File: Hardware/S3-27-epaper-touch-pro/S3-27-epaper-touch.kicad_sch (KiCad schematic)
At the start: 111 parts, among them J1 AFC24-S24FIC-00, J10 Conn_01x06_Pin, J2 Conn_01x06, J3 Conn_01x06, J4 TochConn, J5 Groove sensor, J6 Conn_01x05_Pin, J7 Conn_01x04_Pin, J8 Conn_01x06, Q1 Si1308, Q2 Si2301, SW1 SW_Push, SW2 SW_Push, SW3 SW_Push, SW4 SW_Push, SW5 SW_Push, SW6 SW_Push, SW7 SW_Push, SW8 SW_Push, SW9 SW_Push, U1 ESP32-S3-WROOM-1-N8, U2 RT9013, U3 KoreanHropartsElecTYPE-C-31-M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, U5 BME680, U6 TPL5110, U7 RFM95W-868S2, U8 LSM6DSL

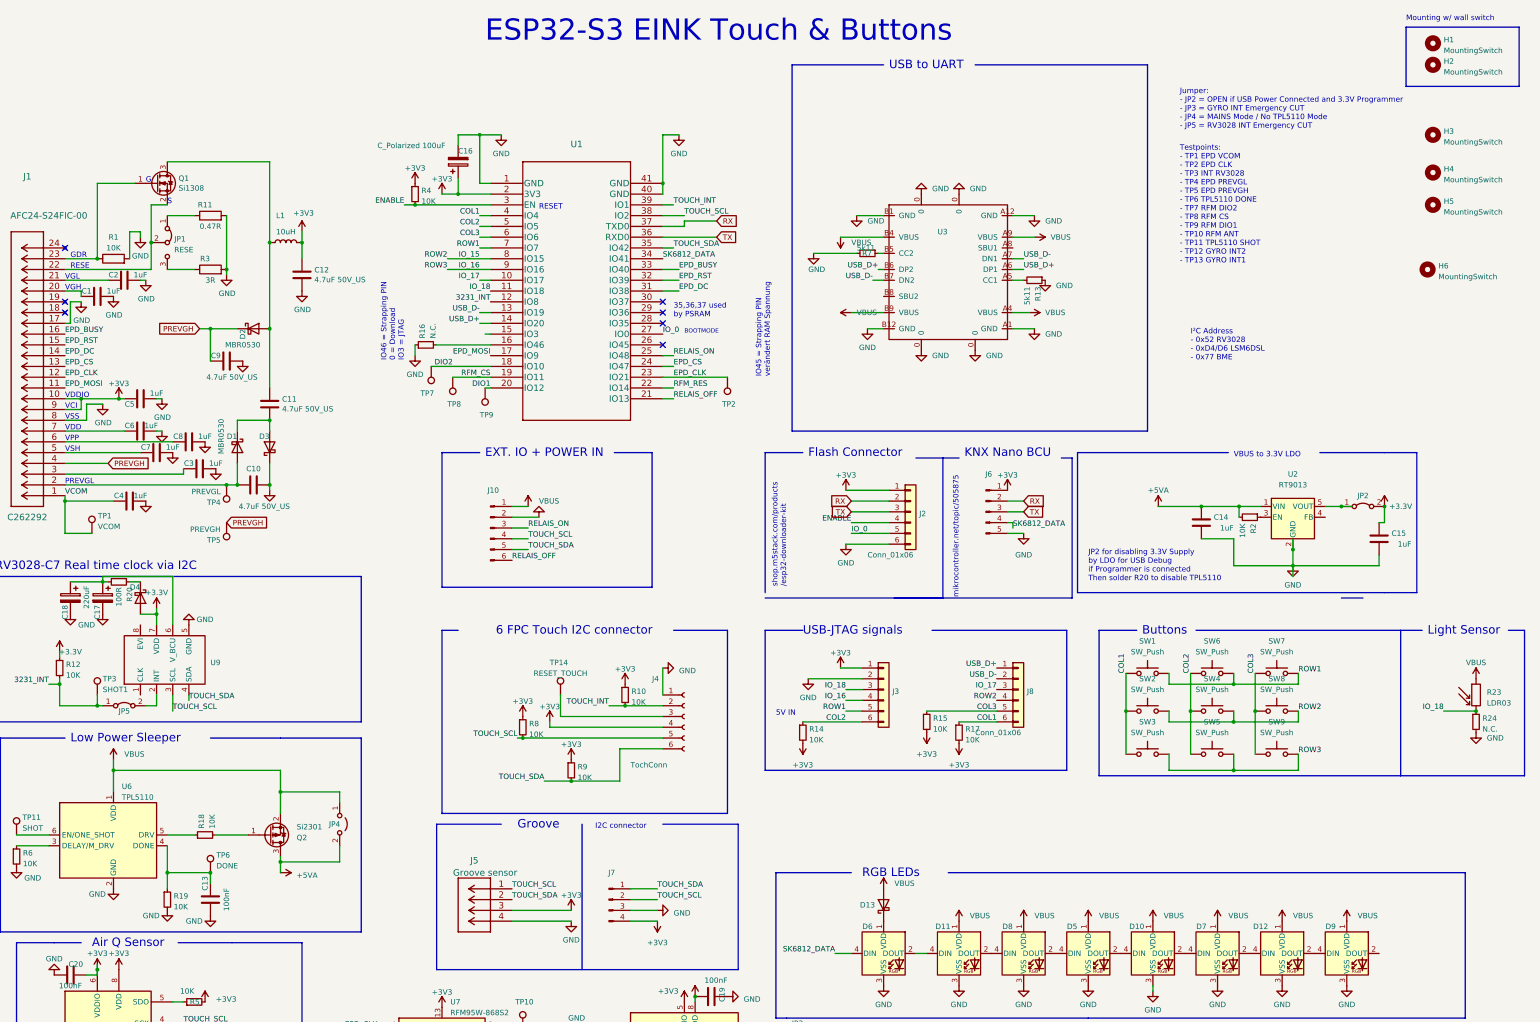
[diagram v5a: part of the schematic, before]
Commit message: Bugfixes for Production
Added a Pin Connector for a Microphone 
Fixed Bug on RV3032/RV3028 for unintended wakeup
Removed Groove Connector due to collission with Touch Controller
Changed Position of BME680
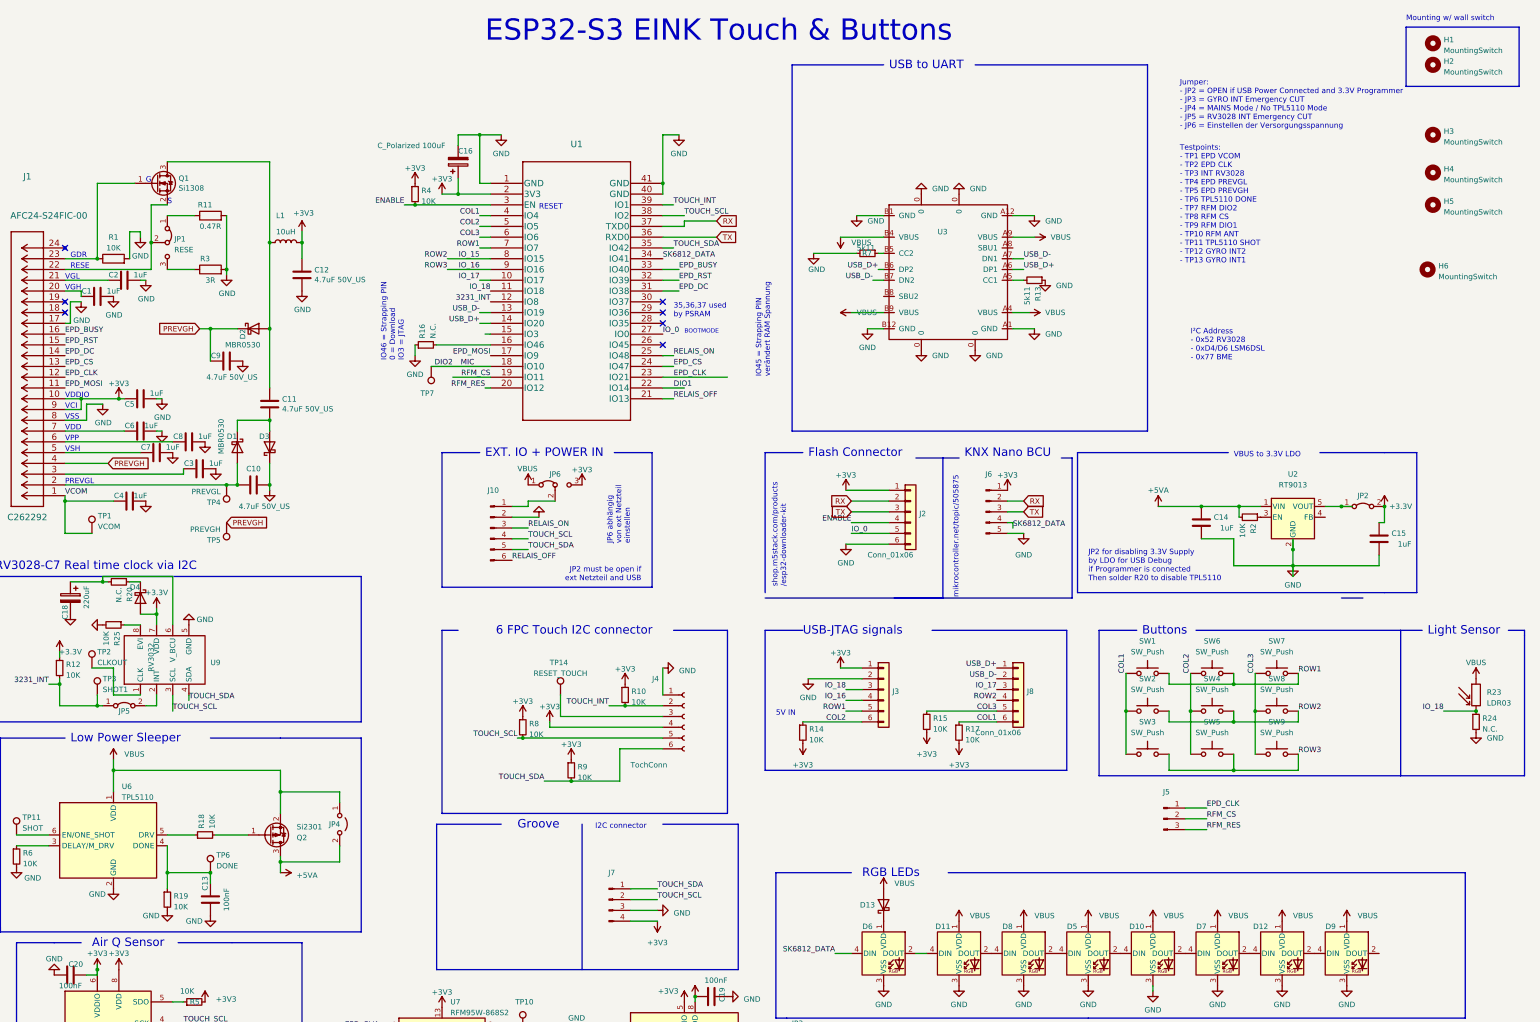
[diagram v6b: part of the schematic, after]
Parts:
- removed C17: 220uF, Capacitor_Tantalum_SMD:CP_EIA-3528-21_Kemet-B, symbol Device:C_Polarized
- removed J5: Groove sensor, footprint:MOLEX-I2C-532530470, symbol MOLEX-I2C-532530470:532530470
- removed TP8, TP9: VCOM, TestPoint:TestPoint_Pad_D1.5mm, symbol Connector:TestPoint
- added J5: Conn_01x03_Pin, Connector_PinHeader_2.54mm:PinHeader_1x03_P2.54mm_Vertical, symbol Connector:Conn_01x03_Pin
- added JP6: Jumper_3_Bridged12, Jumper:SolderJumper-3_P1.3mm_Bridged12_RoundedPad1.0x1.5mm_NumberLabels, symbol Jumper:Jumper_3_Bridged12
- added R25: 10K, Resistor_SMD:R_0805_2012Metric_Pad1.20x1.40mm_HandSolder, symbol Device:R_Small
- R20: value 100R -> N.C.
- TP2: value VCOM -> CLKOUT
- U1: LCSC C2913204 -> (none)
- U9: value ~ -> RV3032
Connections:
- net +3V3: now also JP6.3 (B)
- net DIO1: now also U1.22 (IO14); no longer U1.20 (IO12)
- net EPD_CLK: now also J5.1 (Pin_1); no longer TP2.1
- net GND: now also R25.2
- net RFM_CS: now also J5.2 (Pin_2)
- net RFM_RES: now also U1.20 (IO12), J5.3 (Pin_3); no longer U1.22 (IO14)
- net VBUS: now also JP6.1 (A); no longer J10.1 (Pin_1)
- net at U9.1 (CLK): now also TP2.1
- net at U9.8 (EVI): now also R25.1
- new net: J10.1 (Pin_1), JP6.2 (C)
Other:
- note added: "JP2 must be open if ext Netzteil and USB"
- note added: "JP6 abhängig von ext Netzteil einstellen"
- note added: "Jumper: - JP2 = OPEN if USB Power Connected and 3.3V Programmer - JP3 = GYRO INT Emergency CUT - JP4 = MAINS Mode / No TPL5110 Mode - JP5 = RV3028 INT Emergency CUT - JP6 = Einstellen der Versorgungsspannung"
- note removed: "Jumper: - JP2 = OPEN if USB Power Connected and 3.3V Programmer - JP3 = GYRO INT Emergency CUT - JP4 = MAINS Mode / No TPL5110 Mode - JP5 = RV3028 INT Emergency CUT"

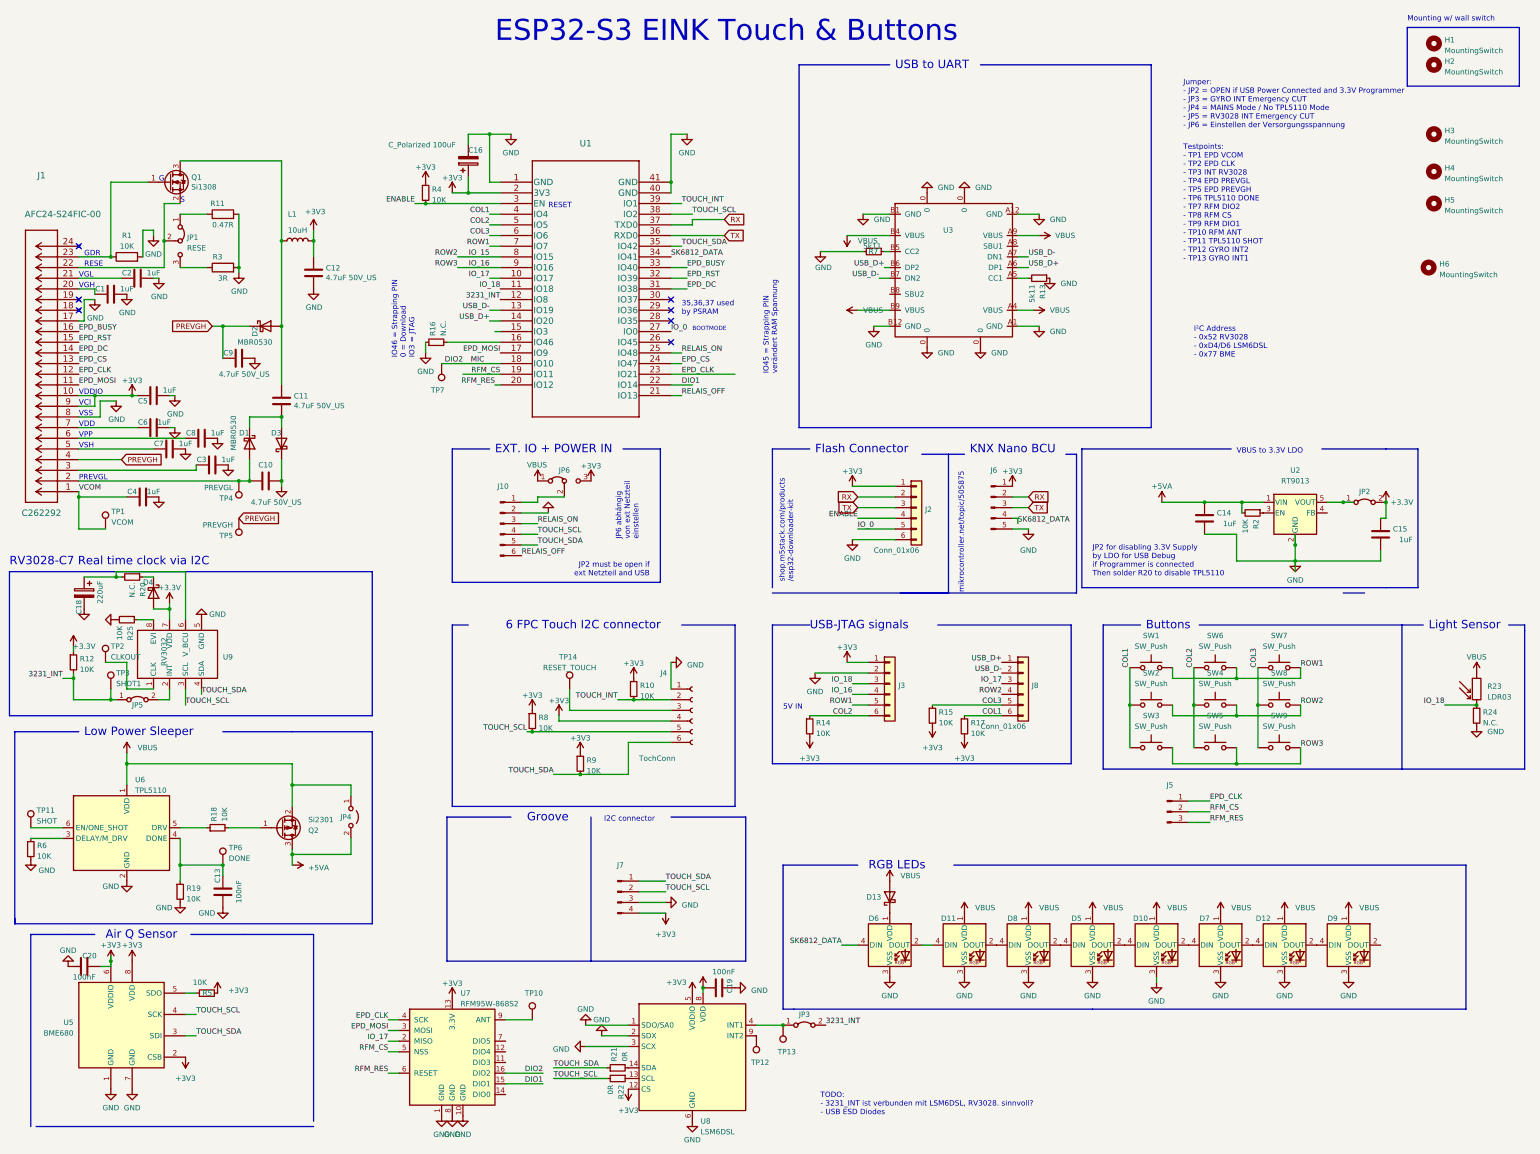
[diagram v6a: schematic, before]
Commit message: Reworked Int Lines of I²C Connections
- Cleaned up Schematic
- added Micorphone Connector
- renamed RFM Miso Pins
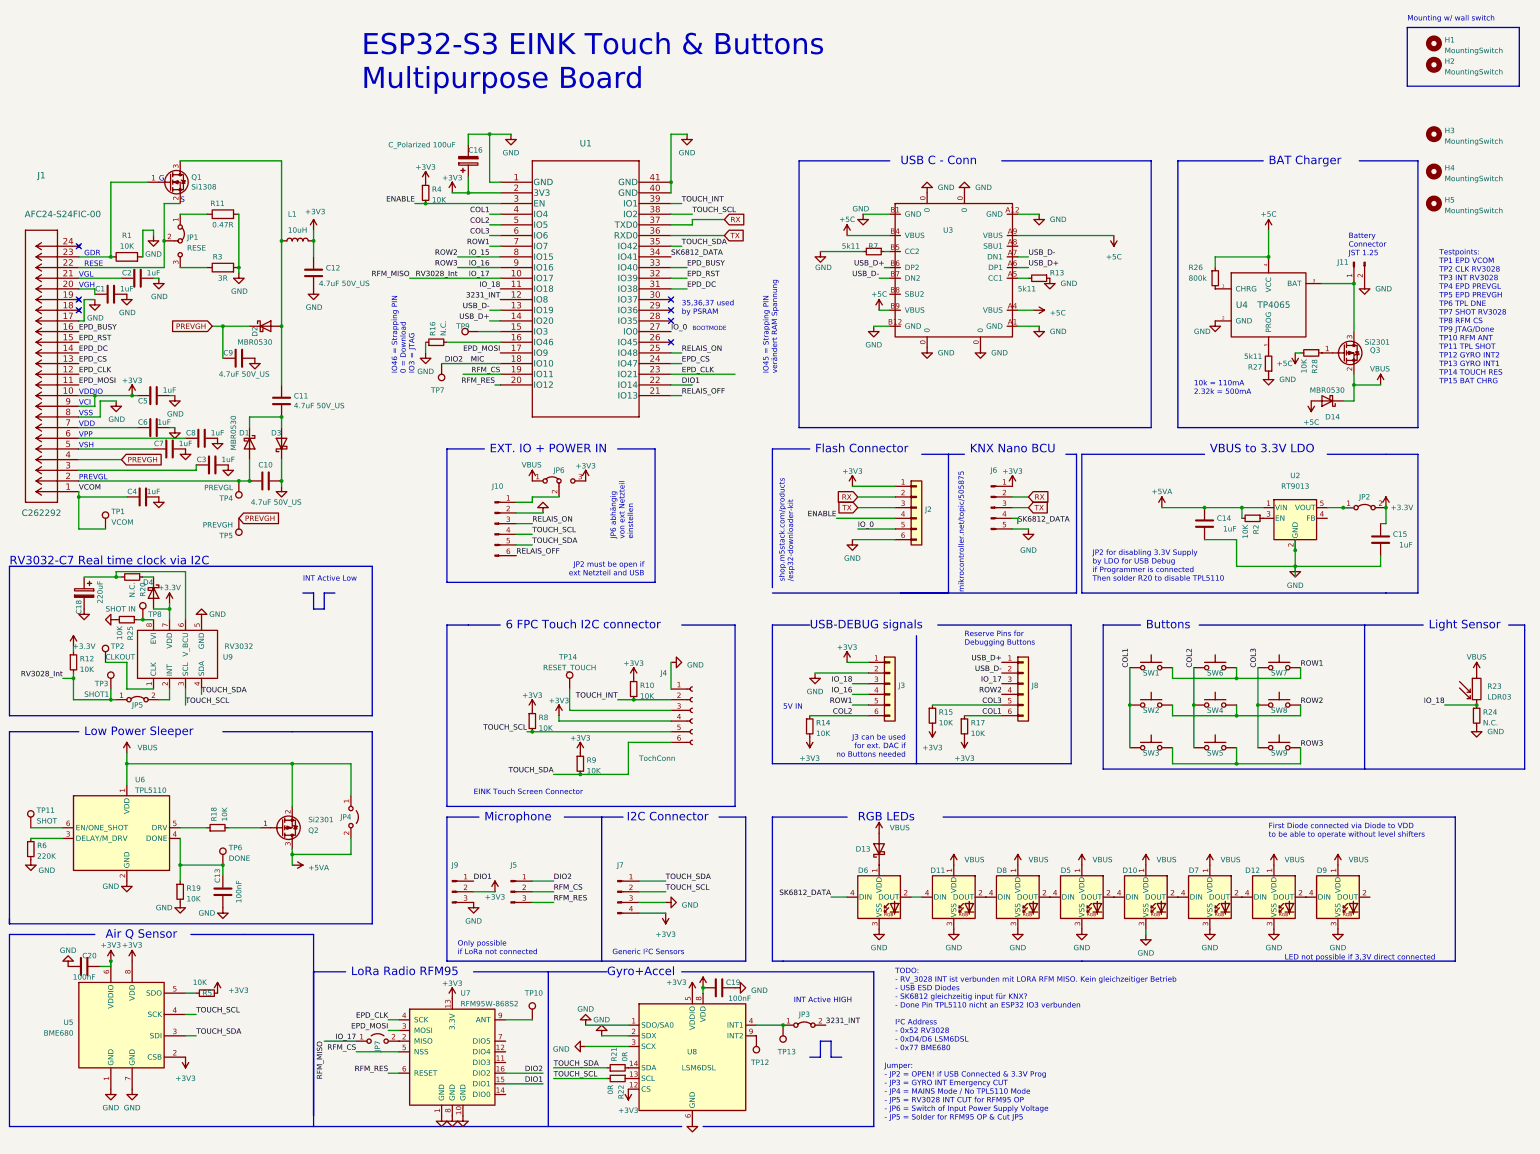
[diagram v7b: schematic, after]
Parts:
- removed H6: MountingSwitch, MountingHole:MountingHole_3.2mm_M3, symbol Mechanical:MountingHole
- added D14: MBR0530, Diode_SMD:D_SOD-123, symbol Diode:MBR0530
- added J11: Conn_01x02_Pin, Connector_JST:JST_GH_SM02B-GHS-TB_1x02-1MP_P1.25mm_Horizontal, symbol Connector:Conn_01x02_Pin
- added J9: Conn_01x03_Pin, Connector_PinHeader_2.54mm:PinHeader_1x03_P2.54mm_Vertical, symbol Connector:Conn_01x03_Pin
- added JP7: Jumper_2_Open, Jumper:SolderJumper-2_P1.3mm_Open_RoundedPad1.0x1.5mm, symbol Jumper:Jumper_2_Open
- added Q3: Si2301, Package_TO_SOT_SMD:SOT-23, symbol Transistor_FET:Si2319CDS
- added R26: 800k, Resistor_SMD:R_0805_2012Metric_Pad1.20x1.40mm_HandSolder, symbol Device:R_Small
- added R27: 5k11, Resistor_SMD:R_0805_2012Metric_Pad1.20x1.40mm_HandSolder, symbol Device:R_Small
- added R28: 10K, Resistor_SMD:R_0805_2012Metric_Pad1.20x1.40mm_HandSolder, symbol Device:R_Small
- added TP8: SHOT IN, TestPoint:TestPoint_Pad_D1.5mm, symbol Connector:TestPoint
- added TP9: VCOM, TestPoint:TestPoint_Pad_D1.5mm, symbol Connector:TestPoint
- added U4: TP4065, tp4056:SOT-23-5_L3.0-W1.7-P0.95-LS2.8-BR, symbol tp4056:TP4065
- R6: value 10K -> 220K; LCSC C17414 -> (none)
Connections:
- net +3V3: now also J9.2 (Pin_2)
- net 3231_INT: no longer JP5.1 (A), R12.2, TP3.1
- net DIO1: now also J9.1 (Pin_1)
- net DIO2: now also J5.1 (Pin_1)
- net EPD_CLK: no longer J5.1 (Pin_1)
- net GND: now also J11.2 (Pin_2), J9.3 (Pin_3), R27.1, U4.2 (GND)
- net IO_17: now also JP5.1 (A), R12.2, TP3.1, JP7.1 (A); no longer U7.2 (MISO)
- net VBUS: now also D14.1 (K), Q3.2 (S); no longer U3.A4 (VBUS), U3.A9 (VBUS), U3.B4 (VBUS), U3.B9 (VBUS)
- net at R25.1, U9.8 (EVI): now also TP8.1
- net at U1.15 (IO3): now also TP9.1
- new net: JP7.2 (B), U7.2 (MISO)
- new net: Q3.1 (G), R28.1
- new net: J11.1 (Pin_1), Q3.3 (D), U4.3 (BAT)
- new net: R26.2, U4.1 (CHRG)
- new net: R27.2, U4.5 (PROG)
- new net +5C: D14.2 (A), R26.1, R28.2, U3.A4 (VBUS), U3.A9 (VBUS), U3.B4 (VBUS), U3.B9 (VBUS), U4.4 (VCC)
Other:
- note added: "10k = 110mA 2.32k = 500mA"
- note added: "BAT Charger"
- note added: "Battery Connector JST 1.25"
- note added: "EINK Touch Screen Connector"
- note added: "ESP32-S3 EINK Touch & Buttons Multipurpose Board"
- note added: "First Diode connected via Diode to VDD to be able to operate without level shifters"
- note added: "Generic I²C Sensors"
- note added: "Gyro+Accel"
- note added: "I2C Connector"
- note added: "INT Active HIGH"
- note added: "INT Active Low"
- note added: "I²C Address - 0x52 RV3028 - 0xD4/D6 LSM6DSL - 0x77 BME680"
- note added: "J3 can be used for ext. DAC if no Buttons needed"
- note added: "Jumper: - JP2 = OPEN! if USB Connected & 3.3V Prog - JP3 = GYRO INT Emergency CUT - JP4 = MAINS Mode / No TPL5110 Mode - JP5 = RV3028 INT CUT for RFM95 OP - JP6 = Switch of Input Power Supply Voltage - JP5 = Solder for RFM95 OP & Cut JP5"
- note added: "LED not possible if 3,3V direct connected"
- note added: "LoRa Radio RFM95"
- note added: "Microphone"
- note added: "Only possible if LoRa not connected"
- note added: "RV3032-C7 Real time clock via I2C"
- note added: "Reserve Pins for Debugging Buttons"
- note added: "TODO: - RV_3028 INT ist verbunden mit LORA RFM MISO. Kein gleichzeitiger Betrieb - USB ESD Diodes - SK6812 gleichzeitig input für KNX? - Done Pin TPL5110 nicht an ESP32 IO3 verbunden"
- note added: "Testpoints: TP1 EPD VCOM TP2 CLK RV3028 TP3 INT RV3028 TP4 EPD PREVGL TP5 EPD PREVGH TP6 TPL DNE TP7 SHOT RV3028 TP8 RFM CS TP9 JTAG/Done TP10 RFM ANT TP11 TPL SHOT TP12 GYRO INT2 TP13 GYRO INT1 TP14 TOUCH RES TP15 BAT CHRG"
- note added: "USB C - Conn"
- note added: "USB-DEBUG signals"
- note removed: "ESP32-S3 EINK Touch & Buttons"
- note removed: "Groove"
- note removed: "I2C connector"
- note removed: "I²C Address - 0x52 RV3028 - 0xD4/D6 LSM6DSL - 0x77 BME"
- note removed: "Jumper: - JP2 = OPEN if USB Power Connected and 3.3V Programmer - JP3 = GYRO INT Emergency CUT - JP4 = MAINS Mode / No TPL5110 Mode - JP5 = RV3028 INT Emergency CUT - JP6 = Einstellen der Versorgungsspannung"
- note removed: "RESET"
- note removed: "RV3028-C7 Real time clock via I2C"
- note removed: "TODO: - 3231_INT ist verbunden mit LSM6DSL, RV3028. sinnvoll? - USB ESD Diodes"
- note removed: "Testpoints: - TP1 EPD VCOM - TP2 EPD CLK - TP3 INT RV3028 - TP4 EPD PREVGL - TP5 EPD PREVGH - TP6 TPL5110 DONE - TP7 RFM DIO2 - TP8 RFM CS - TP9 RFM DIO1 - TP10 RFM ANT - TP11 TPL5110 SHOT - TP12 GYRO INT2 - TP13 GYRO INT1"
- note removed: "USB to UART"
- note removed: "USB-JTAG signals"
- moved on the sheet: C14, C15, D10, D11, D12, D13, D5, D6, D7, D8, D9, J10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

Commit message: Finished for production
Added a dedicated Int Line for each I²C Sensor
Added several TP (GPIO3)
Rotated Battery Connector
Fixed Production files
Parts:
- R26: LCSC C27834 -> (none)
- R3: LCSC C25237 -> (none)
- U4: LCSC (none) -> C113540
- renumbered SW8 to SW3, SW3 to SW4, SW9 to SW5, SW7 to SW6, SW6 to SW7, SW4 to SW8, SW5 to SW9
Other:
- note added: "JP2 must be open if ext PowerSupply and USB is connected"
- note removed: "JP2 must be open if ext Netzteil and USB"
